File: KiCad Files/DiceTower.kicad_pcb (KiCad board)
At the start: 2 copper layers, 2 parts, among them U1 NHD-0420H1Z

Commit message: Add PCB
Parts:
- added C1: 100n, Capacitor_SMD:C_0603_1608Metric, F.Cu at (43.7, 93.5)
- added J1: Conn_02x07_Odd_Even, Connector_PinHeader_2.54mm:PinHeader_2x07_P2.54mm_Vertical, F.Cu at (29.5, 101.1)
- added J2: Conn_01x05_Socket, Connector_PinSocket_2.54mm:PinSocket_1x05_P2.54mm_Vertical, F.Cu at (31.5, 124.0)
- added J3: Conn_01x02_Pin, Connector_PinHeader_2.54mm:PinHeader_1x02_P2.54mm_Vertical, F.Cu at (60.5, 88.4)
- added JP1: Vfeather/Vbatt, Jumper:SolderJumper-3_P1.3mm_Bridged12_RoundedPad1.0x1.5mm_NumberLabels, F.Cu at (24.9, 84.8)
- added JP2: SolderJumper_2_Open, Jumper:SolderJumper-2_P1.3mm_Open_RoundedPad1.0x1.5mm, F.Cu at (24.4, 94.5)
- added R1: 220, PCM_Resistor_SMD_AKL:R_0603_1608Metric, F.Cu at (51.8, 97.5)
- added R10: 10k, PCM_Resistor_SMD_AKL:R_0603_1608Metric, F.Cu at (39.1, 120.4)
- added R11: 10k, PCM_Resistor_SMD_AKL:R_0603_1608Metric, F.Cu at (39.1, 131.8)
- added R12: 18k, PCM_Resistor_SMD_AKL:R_0603_1608Metric, F.Cu at (39.1, 134.6)
- added R13: 10k, PCM_Resistor_SMD_AKL:R_0603_1608Metric, F.Cu at (39.1, 126.1)
- added R14: 18k, PCM_Resistor_SMD_AKL:R_0603_1608Metric, F.Cu at (39.1, 128.9)
- added R2: 10k, PCM_Resistor_SMD_AKL:R_0603_1608Metric, F.Cu at (39.1, 117.6)
- added R3: 10k, PCM_Resistor_SMD_AKL:R_0603_1608Metric, F.Cu at (39.1, 111.9)
- added R4: 10k, PCM_Resistor_SMD_AKL:R_0603_1608Metric, F.Cu at (39.1, 114.8)
- added R5: 10k, PCM_Resistor_SMD_AKL:R_0603_1608Metric, F.Cu at (39.1, 100.6)
- added R6: 10k, PCM_Resistor_SMD_AKL:R_0603_1608Metric, F.Cu at (39.1, 103.4)
- added R7: 10k, PCM_Resistor_SMD_AKL:R_0603_1608Metric, F.Cu at (39.1, 106.3)
- added R8: 10k, PCM_Resistor_SMD_AKL:R_0603_1608Metric, F.Cu at (39.1, 109.1)
- added R9: 18k, PCM_Resistor_SMD_AKL:R_0603_1608Metric, F.Cu at (39.1, 123.3)
- added RV1: R_Potentiometer_Trim, PCM_Potentiometer_THT_AKL:Potentiometer_Bourns_3266W_Vertical, F.Cu at (66.7, 138.2)
- added U3: TPS73131DBV, Package_TO_SOT_SMD:SOT-23-5, F.Cu at (43.7, 90.9)
- U1: footprint Display:NHD-0420H1Z -> Connector_PinHeader_2.54mm:PinHeader_1x16_P2.54mm_Vertical
- moved U1 42.6 mm to (64.1, 132.3), turned to 180 degrees
- moved A1 22.6 mm to (36.2, 91.7), turned to 0 degrees
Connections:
- A1 pad 10: unconnected-(A1-IO4/A5-Pad10) -> /SW2
- A1 pad 11: Net-(A1-SCK/IO5) -> unconnected-(A1-SCK/IO5-Pad11)
- A1 pad 12: Net-(A1-MOSI/IO18) -> /SW0
- A1 pad 13: Net-(A1-MISO/IO19) -> /S2
- A1 pad 14: unconnected-(A1-RX/IO16-Pad14) -> /S1
- A1 pad 15: unconnected-(A1-TX/IO17-Pad15) -> Net-(A1-TX/IO17)
- A1 pad 17: unconnected-(A1-SDA/IO23-Pad17) -> Net-(A1-SDA/IO23)
- A1 pad 18: /DB2 -> Net-(A1-SCL/IO22)
- A1 pad 19: /DB3 -> /DB5
- A1 pad 2: unconnected-(A1-3V3-Pad2) -> +3.3V
- A1 pad 21: /DB5 -> unconnected-(A1-A8/IO15-Pad21)
- A1 pad 24: /DB1 -> unconnected-(A1-A11/IO12-Pad24)
- A1 pad 25: /DB0 -> unconnected-(A1-A12/IO13-Pad25)
- A1 pad 26: +5V -> unconnected-(A1-USB-Pad26)
- A1 pad 27: unconnected-(A1-EN-Pad27) -> Net-(A1-EN)
- A1 pad 28: unconnected-(A1-VBAT-Pad28) -> Net-(A1-VBAT)
- A1 pad 5: unconnected-(A1-DAC2/A0-Pad5) -> /SW3
- A1 pad 6: unconnected-(A1-DAC1/A1-Pad6) -> /SW4
- A1 pad 7: unconnected-(A1-I34/A2-Pad7) -> /SW5
- A1 pad 8: unconnected-(A1-I39/A3-Pad8) -> /SW6
- A1 pad 9: unconnected-(A1-IO36/A4-Pad9) -> /SW1
- U1 pad 10: /DB3 -> unconnected-(U1-DB3-Pad10)
- U1 pad 15: +5V -> +3.3V
- U1 pad 2: +5V -> Net-(JP1-C)
- U1 pad 3: +5V -> Net-(U1-VO)
- U1 pad 4: Net-(A1-SCK/IO5) -> Net-(A1-TX/IO17)
- U1 pad 5: Net-(A1-MOSI/IO18) -> Net-(A1-SDA/IO23)
- U1 pad 6: Net-(A1-MISO/IO19) -> Net-(A1-SCL/IO22)
- U1 pad 7: /DB0 -> unconnected-(U1-DB0-Pad7)
- U1 pad 8: /DB1 -> unconnected-(U1-DB1-Pad8)
- U1 pad 9: /DB2 -> unconnected-(U1-DB2-Pad9)
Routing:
- added copper zone on F.Cu, net GND
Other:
- board outline added: 76.7 x 67.1 mm

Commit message: Octagon
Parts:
- removed J1: Conn_02x07_Odd_Even, Connector_PinHeader_2.54mm:PinHeader_2x07_P2.54mm_Vertical
- removed R10, R11, R13: 10k, PCM_Resistor_SMD_AKL:R_0603_1608Metric
- removed R12, R14, R9: 18k, PCM_Resistor_SMD_AKL:R_0603_1608Metric
- added SW0: ChMxBl, Button_Switch_Keyboard:SW_Cherry_MX_1.00u_PCB, F.Cu at (-33.5, 37.1)
- added SW1: ChMxBl, Button_Switch_Keyboard:SW_Cherry_MX_1.00u_PCB, F.Cu at (37.1, 33.5)
- added SW2: ChMxBl, Button_Switch_Keyboard:SW_Cherry_MX_1.00u_PCB, F.Cu at (49.9, -2.55)
- added SW3: ChMxBl, Button_Switch_Keyboard:SW_Cherry_MX_1.00u_PCB, F.Cu at (33.5, -37.1)
- added SW4: ChMxBl, Button_Switch_Keyboard:SW_Cherry_MX_1.00u_PCB, F.Cu at (-2.55, -49.9)
- added SW5: ChMxBl, Button_Switch_Keyboard:SW_Cherry_MX_1.00u_PCB, F.Cu at (-37.1, -33.5)
- added SW6: ChMxBl, Button_Switch_Keyboard:SW_Cherry_MX_1.00u_PCB, F.Cu at (-49.9, 2.55)
- moved U1 157.9 mm to (4.76, -14.0), turned to -90 degrees
- moved JP1 40.3 mm to (28.4, 125.0)
- moved RV1 38.0 mm to (29.8, 129.0), turned to 90 degrees
- moved R2 15.5 mm to (39.1, 102.1)
- moved R1 13.5 mm to (39.1, 93.0), turned to 0 degrees
- moved R5 9.60 mm to (39.1, 110.2)
- moved R6 9.46 mm to (39.1, 112.9)
- moved R7 9.31 mm to (39.1, 115.6)
- moved R8 9.17 mm to (39.1, 118.3)
- moved JP2 8.19 mm to (32.5, 93.5)
- moved R4 7.26 mm to (39.1, 107.5)
- moved R3 7.12 mm to (39.1, 104.8)
- moved C1 5.11 mm to (43.2, 88.4), turned to 0 degrees
- moved J3 3.31 mm to (60.5, 91.7)
- moved J2 2.09 mm to (32.0, 126.0), turned to 180 degrees
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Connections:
- A1 pad 10: /SW2 -> /SW5
- A1 pad 12: /SW0 -> /SW6
- A1 pad 16: unconnected-(A1-IO21-Pad16) -> /KEY
- A1 pad 19: /DB5 -> /DB4
- A1 pad 20: /DB4 -> /DB5
- A1 pad 5: /SW3 -> /SW0
- A1 pad 6: /SW4 -> /SW1
- A1 pad 7: /SW5 -> /SW2
- A1 pad 8: /SW6 -> /SW3
- A1 pad 9: /SW1 -> /SW4
- J2 pad 2: Net-(J2-Pin_2) -> /KEY
- J2 pad 3: Net-(J2-Pin_3) -> /S1
- J2 pad 4: Net-(J2-Pin_4) -> /S2
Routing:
- net +3.3V: track 0.00 -> 67.9 mm
- net Net-(JP1-B): track 0.00 -> 45.4 mm
- net Net-(JP1-C): track 0.00 -> 44.0 mm
- net Net-(U1-VO): track 0.00 -> 32.1 mm
- net Net-(JP2-B): track 0.00 -> 29.6 mm, vias 0 -> 1
- net Net-(A1-TX/IO17): track 0.00 -> 25.3 mm
- net Net-(A1-VBAT): track 0.00 -> 19.3 mm
- net /DB4: track 0.00 -> 18.5 mm
- net /DB5: track 0.00 -> 16.9 mm
- net /DB7: track 0.00 -> 14.3 mm
- net /DB6: track 0.00 -> 14.3 mm
- net Net-(A1-EN): track 0.00 -> 14.3 mm
- net /KEY: track 0.00 -> 8.08 mm
- net Net-(A1-SDA/IO23): track 0.00 -> 6.72 mm
- net Net-(A1-SCL/IO22): track 0.00 -> 6.72 mm
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- added copper zone on B.Cu, net GND
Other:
- board size 76.7 x 67.1 mm -> 37.1 x 53.3 mm

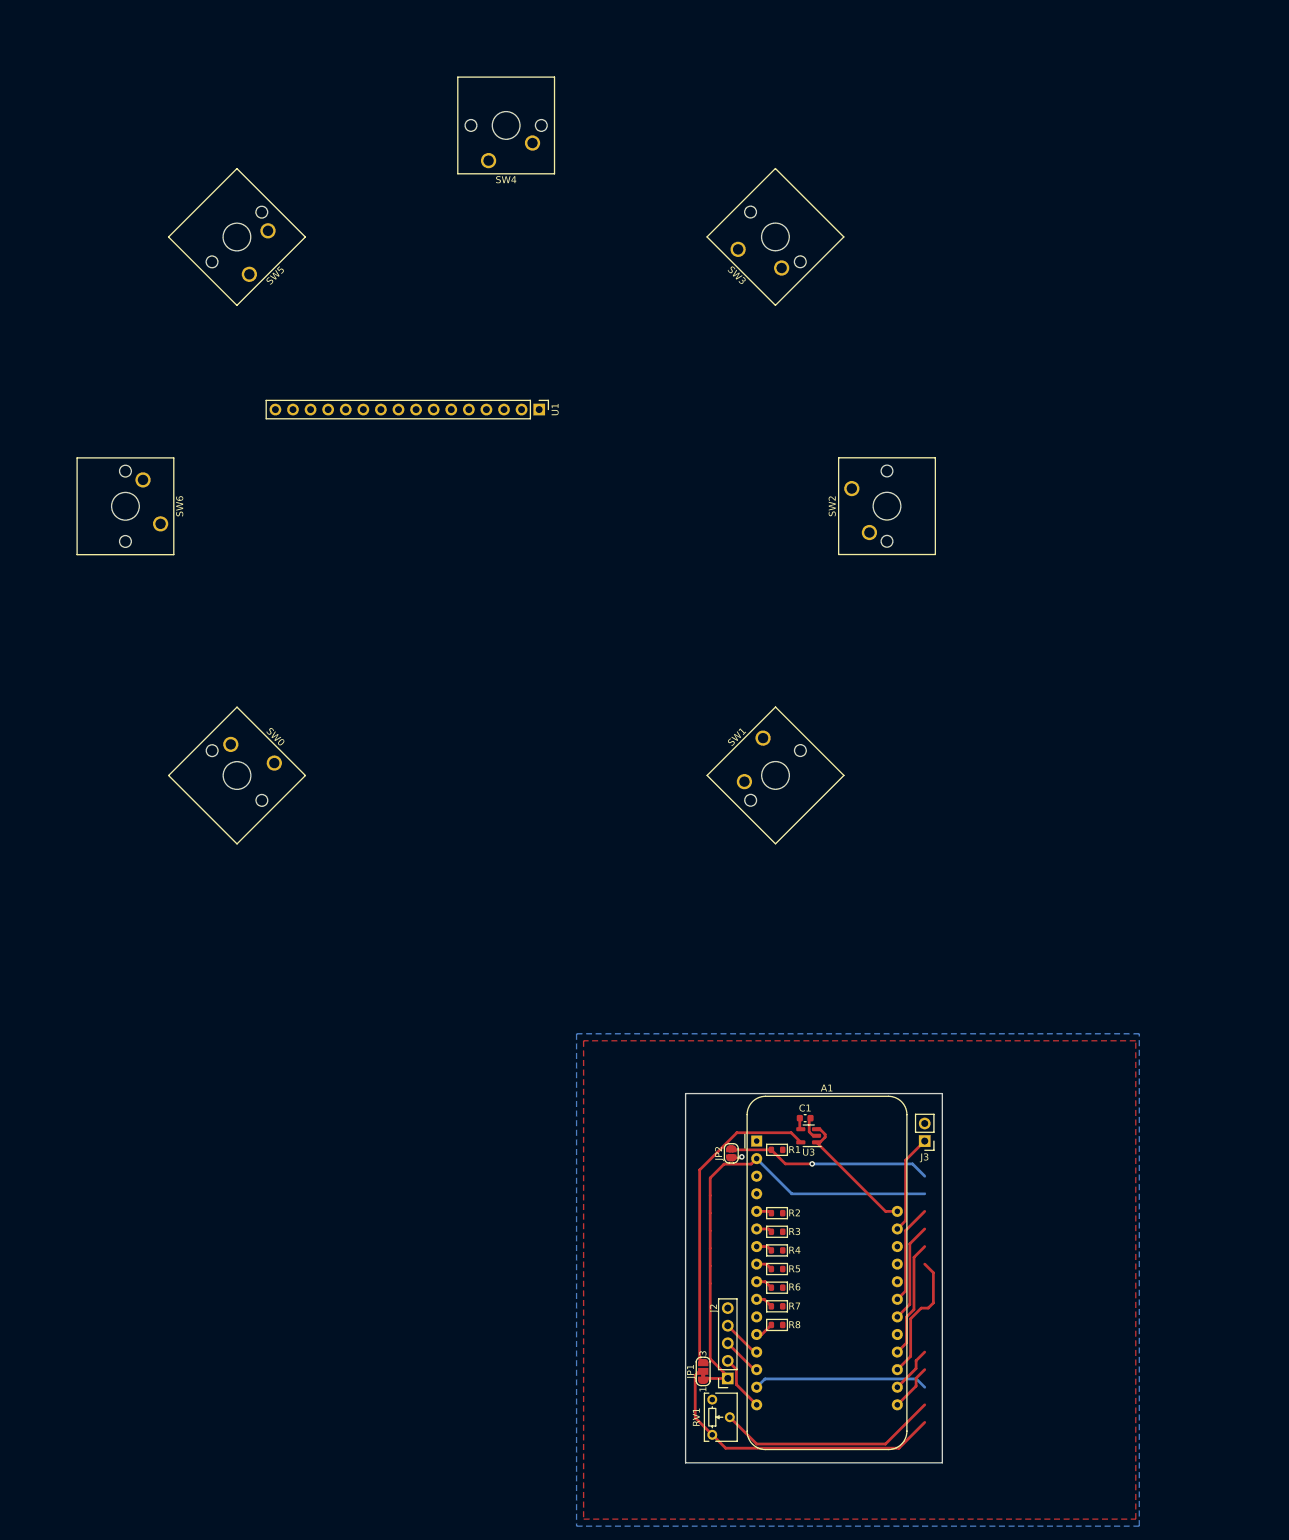
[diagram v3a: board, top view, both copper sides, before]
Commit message: Moved board to key circle
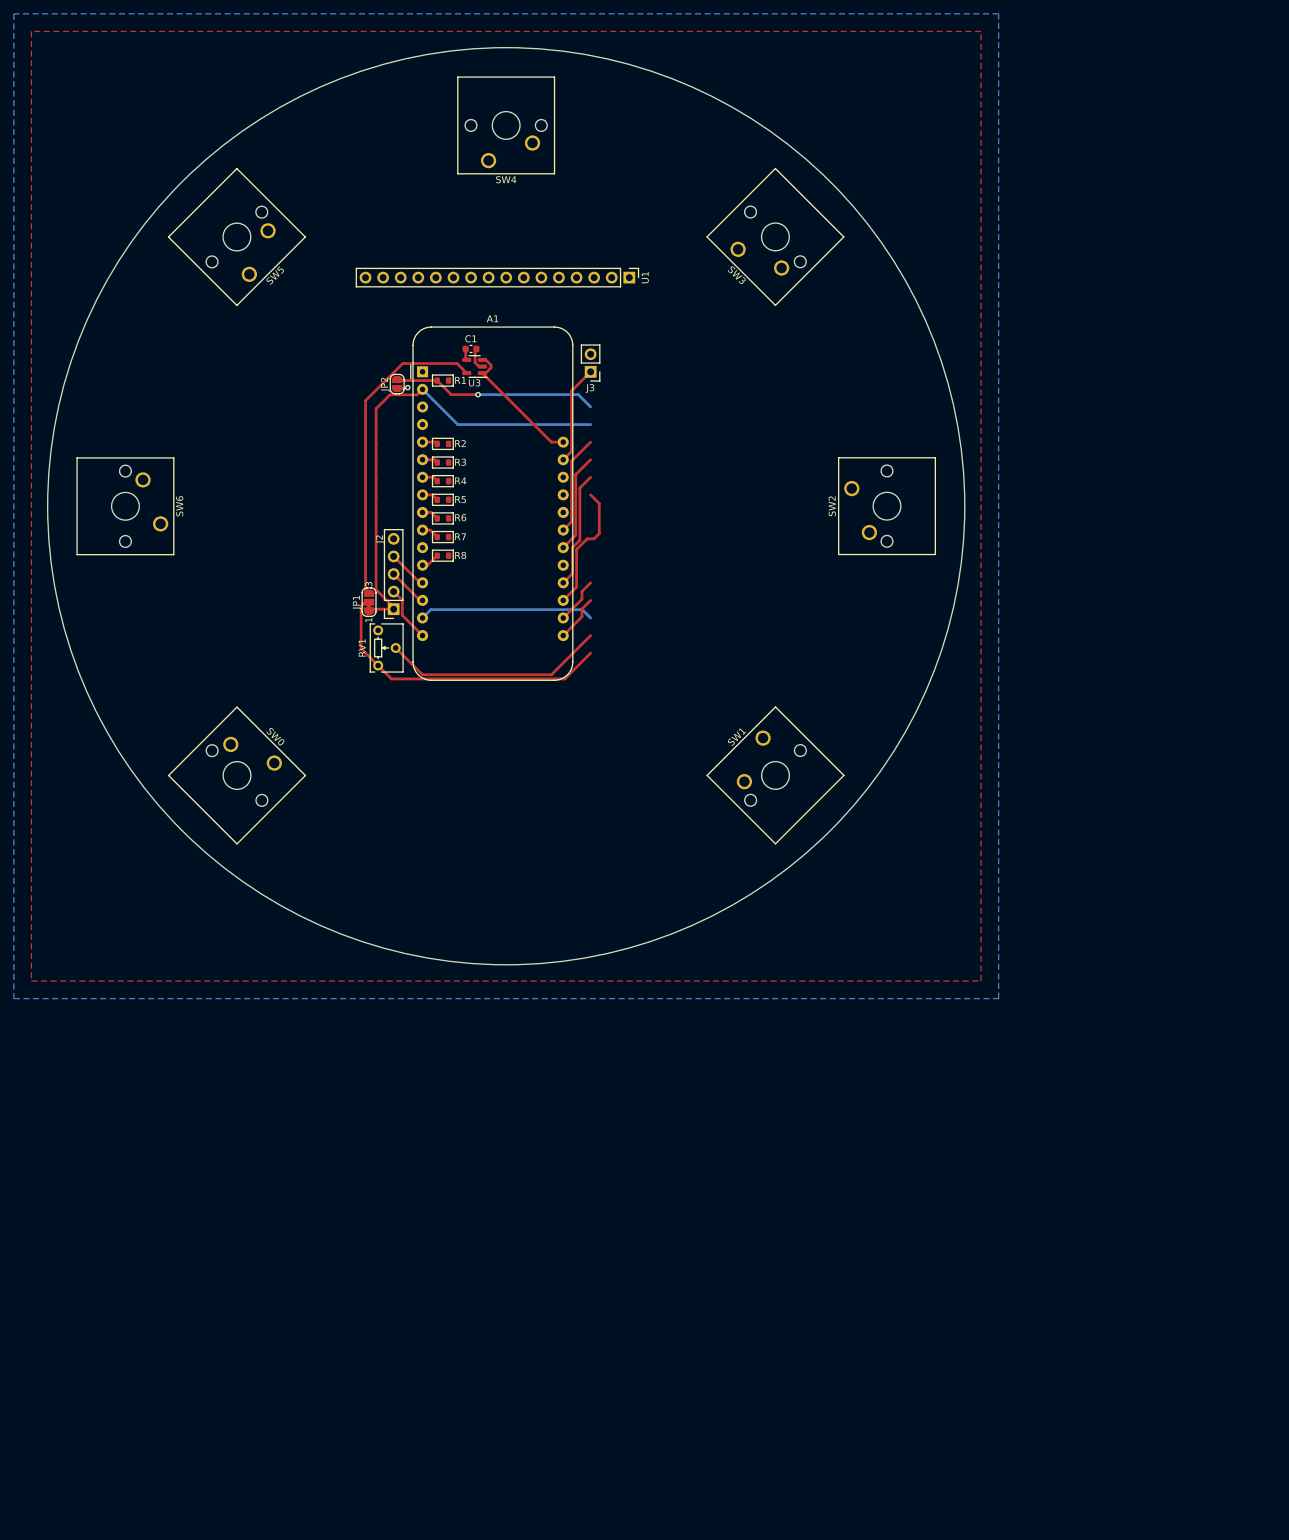
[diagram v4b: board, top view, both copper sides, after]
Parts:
- moved A1 121.1 mm to (-12.1, -19.4)
- moved JP1 121.1 mm to (-19.8, 13.9)
- moved R1 121.1 mm to (-9.14, -18.1)
- moved R2 121.1 mm to (-9.14, -9.00)
- moved R5 121.1 mm to (-9.14, -0.93)
- moved R6 121.1 mm to (-9.14, 1.76)
- moved R8 121.1 mm to (-9.14, 7.15)
- moved U3 121.1 mm to (-4.57, -20.2)
- moved C1 121.1 mm to (-5.08, -22.7)
- moved J2 121.1 mm to (-16.3, 14.9)
- moved J3 121.1 mm to (12.2, -19.4)
- moved JP2 121.1 mm to (-15.7, -17.6)
- moved R3 121.1 mm to (-9.14, -6.31)
- moved R4 121.1 mm to (-9.14, -3.62)
- moved R7 121.1 mm to (-9.14, 4.45)
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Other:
- board size 37.1 x 53.3 mm -> 132.5 x 132.5 mm

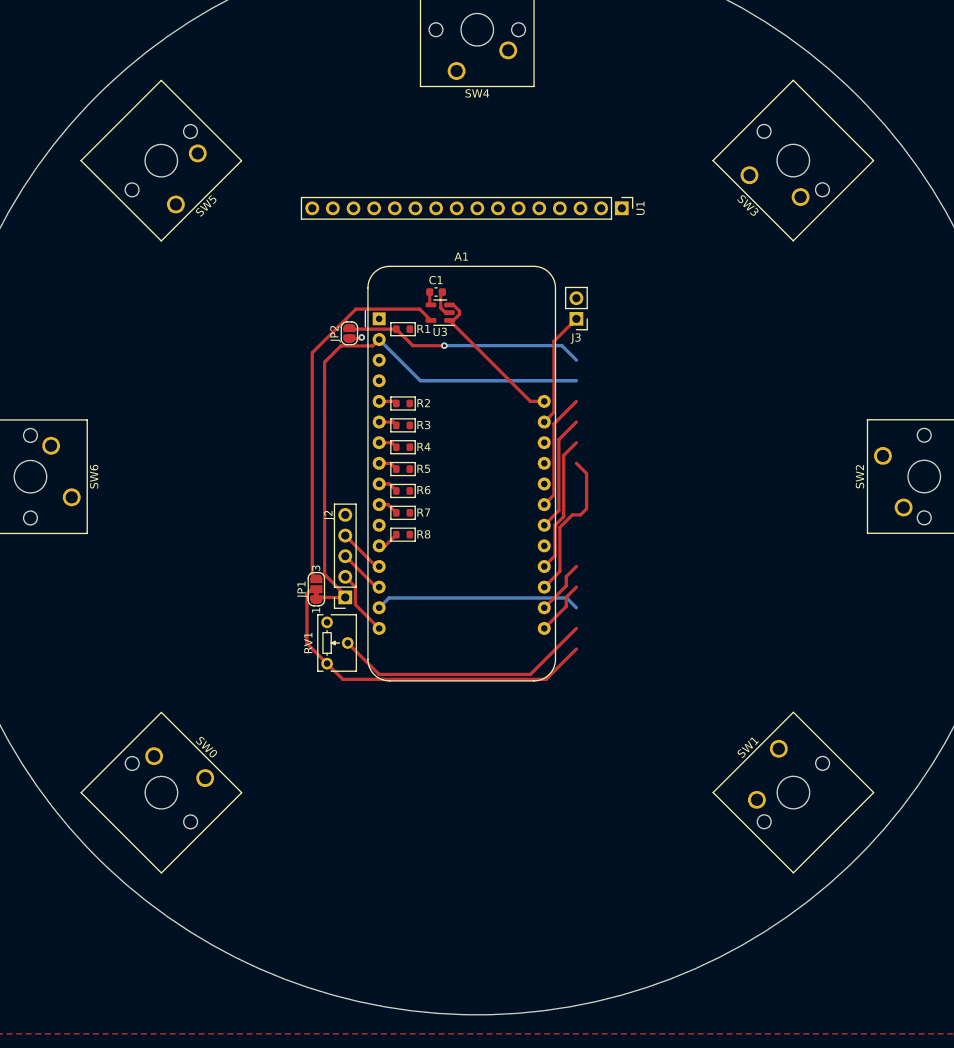
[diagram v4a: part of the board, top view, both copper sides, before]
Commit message: Added usb-c connector
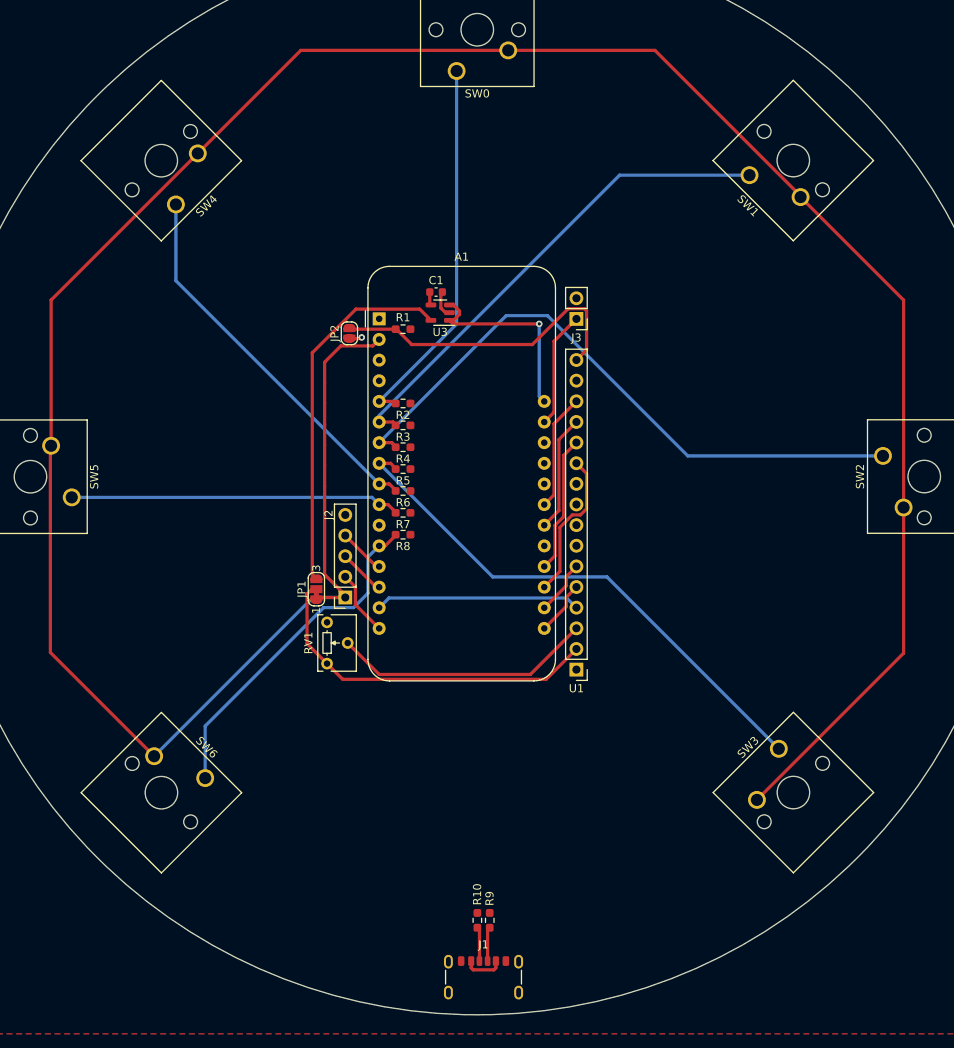
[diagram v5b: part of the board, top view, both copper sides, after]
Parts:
- added J1: USB_C_Receptacle_PowerOnly_6P, Connector_USB:USB_C_Receptacle_GCT_USB4125-xx-x-0190_6P_TopMnt_Horizontal, F.Cu at (0.76, 62.7)
- added R10: 5k1, Resistor_SMD:R_0603_1608Metric_Pad0.98x0.95mm_HandSolder, F.Cu at (0.00, 54.6)
- added R9: 5k1, Resistor_SMD:R_0603_1608Metric_Pad0.98x0.95mm_HandSolder, F.Cu at (1.52, 54.6)
- R1, R2, R3, R4, R5, R6, R7, R8: footprint PCM_Resistor_SMD_AKL:R_0603_1608Metric -> Resistor_SMD:R_0603_1608Metric_Pad0.98x0.95mm_HandSolder
- moved U1 57.0 mm to (12.2, 23.7), turned to 180 degrees
- renumbered SW4 to SW0, SW3 to SW1, SW1 to SW3, SW5 to SW4, SW6 to SW5, SW0 to SW6
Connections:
- A1 pad 26: unconnected-(A1-USB-Pad26) -> Net-(A1-USB)
- SW0 pad 1: /SW4 -> /SW0
- SW1 pad 1: /SW3 -> /SW1
- SW3 pad 1: /SW1 -> /SW3
- SW4 pad 1: /SW5 -> /SW4
- SW5 pad 1: /SW6 -> /SW5
- SW6 pad 1: /SW0 -> /SW6
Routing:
- net +3.3V: track 67.9 -> 334.1 mm
- net /SW2: track 2.35 -> 78.0 mm
- net /SW3: track 2.41 -> 66.1 mm
- net /SW1: track 2.28 -> 60.9 mm
- net /SW4: track 2.47 -> 47.2 mm
- net /SW0: track 2.22 -> 46.8 mm
- net /SW6: track 2.69 -> 42.3 mm
- net /SW5: track 2.53 -> 40.7 mm
- net Net-(JP2-B): track 29.6 -> 38.5 mm, vias 1 -> 0
- net Net-(A1-VBAT): track 19.3 -> 24.5 mm, vias 0 -> 1
- net Net-(A1-USB): track 0.00 -> 4.92 mm
- net Net-(J1-CC2): track 0.00 -> 4.21 mm
- net Net-(J1-CC1): track 0.00 -> 4.21 mm

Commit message: Finish PCB
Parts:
- moved R8 0.38 mm to (-8.89, 6.86)
- moved R4 0.38 mm to (-8.89, -3.91)
- moved R6 0.38 mm to (-8.89, 1.48)
- moved R5 0.38 mm to (-8.89, -1.22)
- moved R2 0.38 mm to (-8.89, -9.29)
- moved R3 0.38 mm to (-8.89, -6.60)
- moved R7 0.38 mm to (-8.89, 4.17)
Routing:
- net +3.3V: track 334.1 -> 454.7 mm, vias 0 -> 1
- net Net-(A1-USB): track 4.92 -> 71.2 mm
- net /SW2: track 78.0 -> 65.6 mm
- net /SW3: track 66.1 -> 71.7 mm, vias 0 -> 1
- net GND: track 4.93 -> 8.71 mm, vias 1 -> 23
- net Net-(U1-VO): track 32.1 -> 29.6 mm
